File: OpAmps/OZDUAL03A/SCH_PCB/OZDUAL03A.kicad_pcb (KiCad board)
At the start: 2 copper layers, 40.4 x 40.4 mm, 53 parts, among them Con1 47u, Con2 47u, Con3 47u, Con4 47u, J1 JUMP2_2x1, J2 POWER, J3 OPAMPA, J4 OPAMPB, J5 SOT23-6, M1 HOLE, M2 HOLE, M3 HOLE, M4 HOLE, U1 OZ, U2 sot23-6

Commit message: Oprava, generování dat
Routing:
- net /VIN-: track 27.6 -> 30.9 mm
- net GNDA: track 198.2 -> 199.0 mm
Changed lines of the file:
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@@
-(kicad_pcb (version 4) (host pcbnew 4.0.5+dfsg1-4~bpo8+1)
+(kicad_pcb (version 20170123) (host pcbnew "(2017-02-05 revision 431abcf)-makepkg")
   (general
     (links 120)
     (no_connects 0)
-    (area 127.051999 76.251999 167.588001 116.788001)
+    (area 126.56552 69.817 180.212001 118.270714)
     (thickness 1.6)
     (drawings 48)
-    (tracks 401)
+    (tracks 412)
     (zones 0)
     (modules 53)
@@
   )
   (setup
-    (last_trace_width 0.254)
+    (last_trace_width 0.508)
     (user_trace_width 0.254)
     (user_trace_width 0.4572)
@@
     (visible_elements 7FFFFFFF)
     (pcbplotparams
-      (layerselection 0x011f0_80000001)
+      (layerselection 0x011f0_ffffffff)
       (usegerberextensions false)
       (excludeedgelayer true)
@@
       (hpglpenspeed 20)
       (hpglpendiameter 15)
-      (hpglpenoverlay 2)
       (psnegative false)
       (psa4output false)
@@
       (effects (font (size 1.5 1.5) (thickness 0.15)))
     )
-    (fp_text value POWER (at -3.556 0 360) (layer F.SilkS) hide
+    (fp_text value POWER (at -3.556 0) (layer F.SilkS) hide
       (effects (font (size 1.5 1.5) (thickness 0.15)))
     )
@@
     (tags "Diode SMA")
     (attr smd)
-    (fp_text reference Di1 (at -4.445 0 360) (layer F.SilkS)
+    (fp_text reference Di1 (at -4.445 0) (layer F.SilkS)
       (effects (font (size 1 1) (thickness 0.25)))
     )
@@
   (module Mlab_IO:SOT-23-6 (layer F.Cu)
     (at 147.193 105.664 270)
-    (fp_text reference U2 (at 1.99898 0 360) (layer F.SilkS) hide
+    (fp_text reference U2 (at 1.99898 0) (layer F.SilkS) hide
       (effects (font (size 0.762 0.762) (thickness 0.0762)))
     )
@@
   (segment (start 155.60802 83.947) (end 156.21 84.54898) (width 0.635) (layer F.Cu) (net 4))
   (segment (start 147.32 80.01) (end 147.32 82.55) (width 1.016) (layer F.Cu) (net 4))
+  (segment (start 163.83 91.44) (end 163.84 91.43) (width 0.508) (layer F.Cu) (net 5))
+  (segment (start 163.84 91.43) (end 165.19 91.43) (width 0.508) (layer F.Cu) (net 5))
+  (segment (start 165.19 91.43) (end 165.1635 91.4565) (width 0.508) (layer F.Cu) (net 5))
+  (segment (start 165.1635 91.4565) (end 165.1635 102.87) (width 0.508) (layer F.Cu) (net 5))
+  (segment (start 165.1635 102.87) (end 161.671 106.3625) (width 0.508) (layer F.Cu) (net 5))
+  (segment (start 161.671 106.3625) (end 158.75 106.3625) (width 0.508) (layer F.Cu) (net 5))
+  (segment (start 158.75 106.3625) (end 158.75 109.22) (width 0.508) (layer F.Cu) (net 5))
   (segment (start 143.51 102.1715) (end 143.256 102.1715) (width 0.508) (layer F.Cu) (net 5))
   (segment (start 143.256 102.1715) (end 142.24 103.1875) (width 0.508) (layer F.Cu) (net 5))
   (segment (start 142.24 103.1875) (end 142.24 105.3465) (width 0.508) (layer F.Cu) (net 5))
   (segment (start 142.24 105.3465) (end 140.97 106.6165) (width 0.508) (layer F.Cu) (net 5))
-  (segment (start 163.83 91.44) (end 165.1635 92.7735) (width 0.508) (layer F.Cu) (net 5))
-  (segment (start 161.671 106.3625) (end 158.75 106.3625) (width 0.508) (layer F.Cu) (net 5))
-  (segment (start 165.1635 102.87) (end 161.671 106.3625) (width 0.508) (layer F.Cu) (net 5))
-  (segment (start 165.1635 92.7735) (end 165.1635 102.87) (width 0.508) (layer F.Cu) (net 5))
   (segment (start 156.21 101.9175) (end 156.1465 101.9175) (width 0.508) (layer F.Cu) (net 5))
   (segment (start 156.1465 101.9175) (end 154.94 103.124) (width 0.508) (layer F.Cu) (net 5))
@@
   (via (at 154.94 89.916) (size 0.8) (drill 0.4) (layers F.Cu B.Cu) (net 5))
   (segment (start 154.94 89.916) (end 154.94 89.916) (width 0.635) (layer B.Cu) (net 5))
-  (segment (start 158.75 106.3625) (end 158.75 109.22) (width 0.508) (layer F.Cu) (net 5))
   (segment (start 158.75 109.22) (end 158.75 109.093) (width 0.45) (layer F.Cu) (net 5))
   (segment (start 157.48 110.49) (end 157.48 109.1565) (width 0.45) (layer F.Cu) (net 5))
@@
   (segment (start 142.24 80.01) (end 142.24 81.28) (width 1.016) (layer F.Cu) (net 5))
   (segment (start 142.24 81.28) (end 142.24 82.55) (width 1.016) (layer F.Cu) (net 5))
-  (segment (start 137.16 110.49) (end 137.16 109.4105) (width 0.508) (layer F.Cu) (net 6))
-  (segment (start 143.51 107.188) (end 143.51 106.3625) (width 0.508) (layer F.Cu) (net 6))
-  (segment (start 141.9225 108.7755) (end 143.51 107.188) (width 0.508) (layer F.Cu) (net 6))
-  (segment (start 137.795 108.7755) (end 141.9225 108.7755) (width 0.508) (layer F.Cu) (net 6))
-  (segment (start 137.16 109.4105) (end 137.795 108.7755) (width 0.508) (layer F.Cu) (net 6))
+  (segment (start 143.51 106.6165) (end 143.3195 106.6165) (width 0.508) (layer F.Cu) (net 6))
+  (segment (start 143.3195 106.6165) (end 141.316 108.62) (width 0.508) (layer F.Cu) (net 6))
+  (segment (start 141.316 108.62) (end 137.76 108.62) (width 0.508) (layer F.Cu) (net 6))
+  (segment (start 137.76 108.62) (end 137.16 109.22) (width 0.508) (layer F.Cu) (net 6))
+  (segment (start 137.16 109.22) (end 137.16 110.49) (width 0.508) (layer F.Cu) (net 6))
   (segment (start 148.336 94.615) (end 148.336 94.869) (width 0.635) (layer B.Cu) (net 6))
   (segment (start 137.16 109.22) (end 137.16 110.49) (width 0.635) (layer B.Cu) (net 6))
@@
   (segment (start 150.1775 87.58174) (end 149.87524 87.884) (width 0.635) (layer F.Cu) (net 6))
   (segment (start 150.1775 87.58174) (end 149.87524 87.884) (width 0.635) (layer F.Cu) (net 6))
+  (segment (start 144.14 83.91398) (end 143.85 83.91398) (width 0.635) (layer F.Cu) (net 7))
+  (segment (start 143.85 83.91398) (end 138.43 83.91398) (width 0.635) (layer F.Cu) (net 7))
+  (segment (start 144.78 82.7) (end 143.85 83.63) (width 0.508) (layer F.Cu) (net 7))
+  (segment (start 143.85 83.63) (end 143.85 83.91398) (width 0.508) (layer F.Cu) (net 7))
+  (segment (start 144.78 82.55) (end 144.78 82.7) (width 0.508) (layer F.Cu) (net 7))
+  (segment (start 144.55902 83.91398) (end 144.14 83.91398) (width 0.635) (layer F.Cu) (net 7))
+  (segment (start 144.78 83.15) (end 144.14 83.79) (width 0.508) (layer F.Cu) (net 7))
+  (segment (start 144.14 83.79) (end 144.14 83.91398) (width 0.508) (layer F.Cu) (net 7))
+  (segment (start 144.78 82.55) (end 144.78 83.15) (width 0.508) (layer F.Cu) (net 7))
   (segment (start 137.46 86.4) (end 136.12876 87.73124) (width 0.508) (layer F.Cu) (net 7))
   (segment (start 136.12876 87.73124) (end 136.12876 87.884) (width 0.4572) (layer F.Cu) (net 7))
@@
   (segment (start 144.78 83.439) (end 145.669 84.328) (width 1.016) (layer B.Cu) (net 7))
   (segment (start 144.78 82.55) (end 144.78 83.693) (width 0.635) (layer F.Cu) (net 7))
-  (segment (start 144.55902 83.91398) (end 138.43 83.91398) (width 0.635) (layer F.Cu) (net 7))
   (segment (start 138.43 83.91398) (end 138.43 84.59724) (width 0.635) (layer F.Cu) (net 7))
   (segment (start 149.86 80.01) (end 149.86 82.55) (width 1.016) (layer F.Cu) (net 7))
@@
   (segment (start 151.13 100.0125) (end 151.13 99.949) (width 0.635) (layer F.Cu) (net 14))
   (segment (start 161.29 99.06) (end 163.83 99.06) (width 1.016) (layer F.Cu) (net 14))
-  (segment (start 139.7 110.49) (end 139.7 109.855) (width 0.635) (layer B.Cu) (net 15))
-  (segment (start 139.7 109.855) (end 146.05 103.505) (width 0.635) (layer B.Cu) (net 15))
+  (segment (start 139.72 110.49) (end 146.05 104.16) (width 0.508) (layer B.Cu) (net 15))
+  (segment (start 146.05 104.16) (end 146.05 103.505) (width 0.508) (layer B.Cu) (net 15))
+  (segment (start 139.7 110.49) (end 139.72 110.49) (width 0.508) (layer B.Cu) (net 15))
   (via (at 146.05 103.505) (size 0.8) (drill 0.4) (layers F.Cu B.Cu) (net 15))
   (segment (start 146.05 104.5845) (end 146.05 104.267) (width 0.508) (layer F.Cu) (net 15) (status 10))

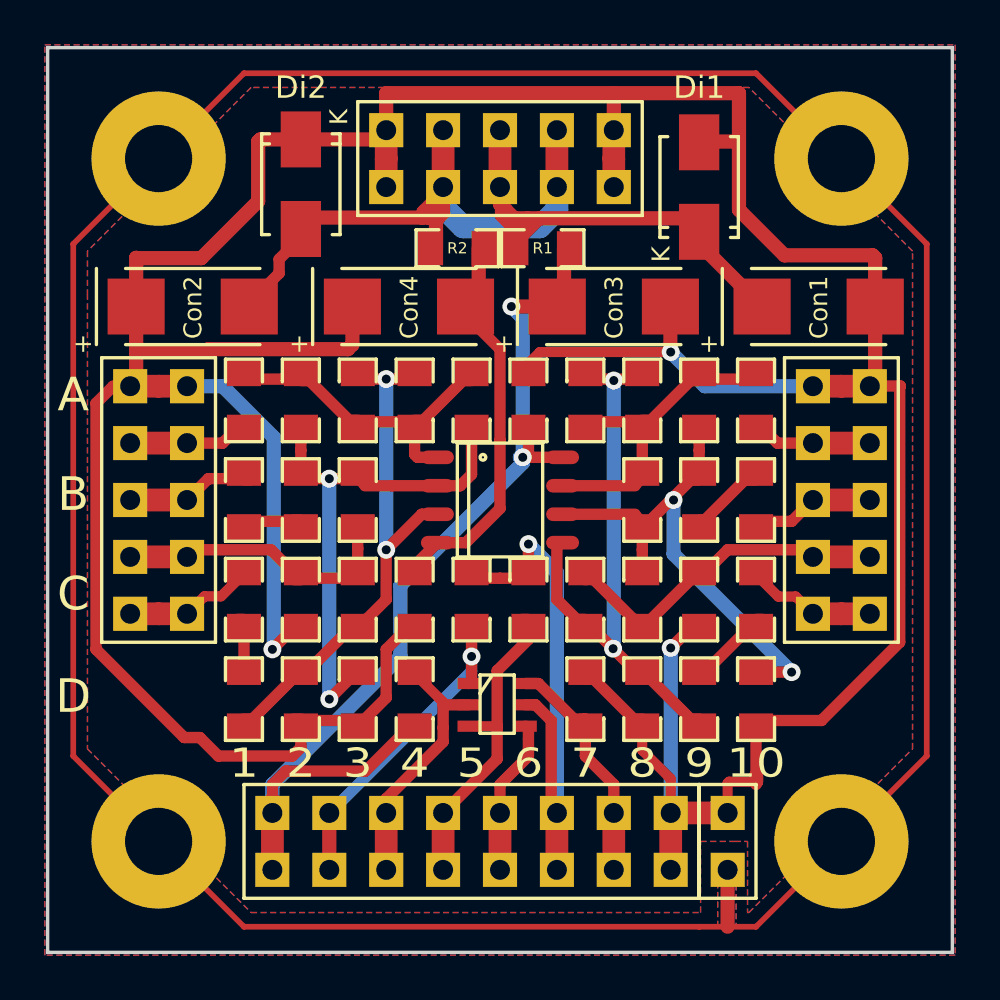
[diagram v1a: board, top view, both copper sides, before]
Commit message: OZDUAL03A module directory reverted to the condition before development of B  module revision.
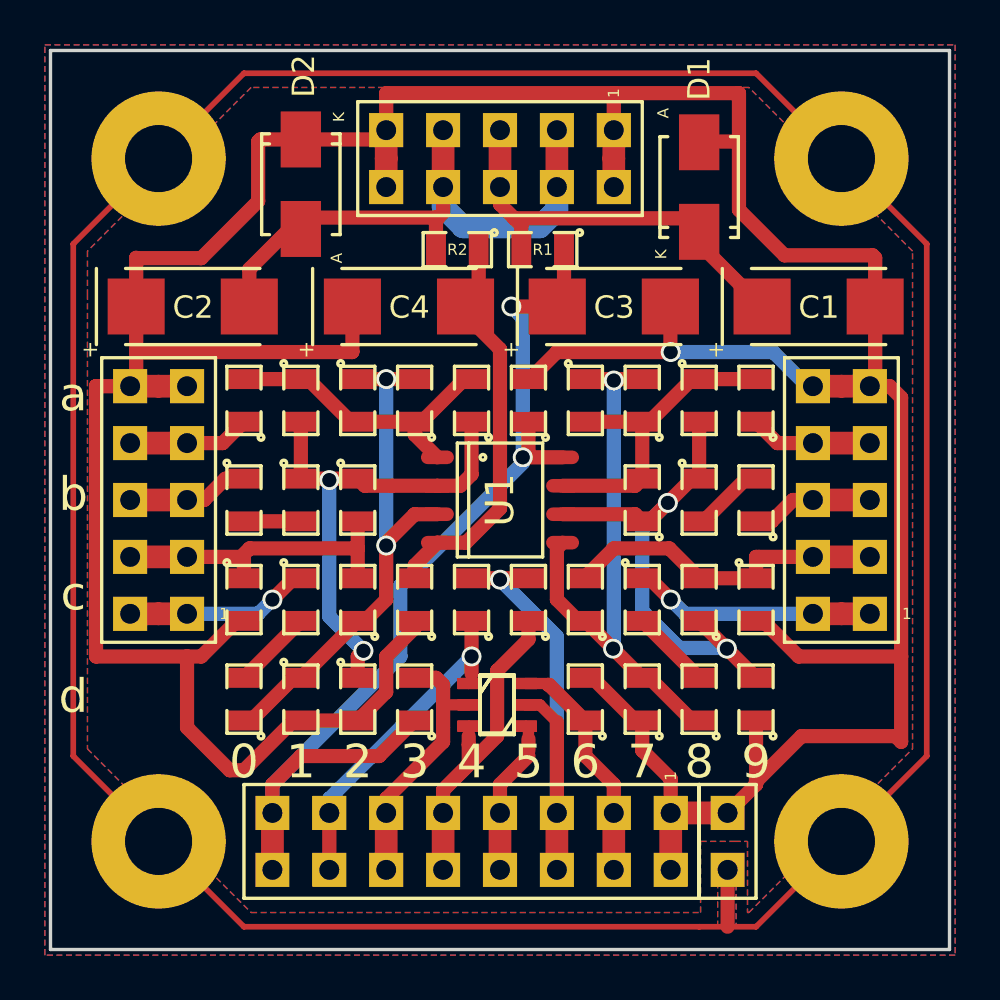
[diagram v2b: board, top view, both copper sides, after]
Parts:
- removed A1, A10, A3, A5, A7, B1, B10, B8, C10, C5, C6, C9: C, Mlab_R:SMD-0805-hand-soldering
- removed A2, A4, A8, A9, B2, B3, B9, C7, C8, D10, D3, D4, D7, D8, D9: R, Mlab_R:SMD-0805-hand-soldering
- removed A6: 100nF, Mlab_R:SMD-0805-hand-soldering
- removed the C1 at (135.9, 101.0)
- removed the C2 at (138.4, 101.0)
- removed the C3 at (141.0, 101.0)
- removed the C4 at (143.5, 101.0)
- removed the D1 at (135.9, 105.4)
- removed the D2 at (138.4, 105.4)
- added Q1: BC846, sot23-6:SOT-23-3, F.Cu at (147.2, 105.7)
- added U3: ANALOG SWITCH, Mlab_IO:SOT-23-6, F.Cu at (147.2, 105.7)
- added a0: C, Mlab_R:SMD-0805, F.Cu at (135.9, 92.1)
- added a1: R, Mlab_R:SMD-0805, F.Cu at (138.4, 92.1)
- added a2: C, Mlab_R:SMD-0805, F.Cu at (141.0, 92.1)
- added a3: R, Mlab_R:SMD-0805, F.Cu at (143.5, 92.1)
- added a4: C, Mlab_R:SMD-0805, F.Cu at (146.1, 92.1)
- added a5: 100nF, Mlab_R:SMD-0805, F.Cu at (148.6, 92.1)
- added a6: C, Mlab_R:SMD-0805, F.Cu at (151.1, 92.1)
- added a7: R, Mlab_R:SMD-0805, F.Cu at (153.7, 92.1)
- added a8: R, Mlab_R:SMD-0805, F.Cu at (156.2, 92.1)
- added a9: C, Mlab_R:SMD-0805, F.Cu at (158.8, 92.1)
- added b0: C, Mlab_R:SMD-0805, F.Cu at (135.9, 96.5)
- added b1: R, Mlab_R:SMD-0805, F.Cu at (138.4, 96.5)
- added b2: R, Mlab_R:SMD-0805, F.Cu at (141.0, 96.5)
- added b7: C, Mlab_R:SMD-0805, F.Cu at (153.7, 96.5)
- added b8: R, Mlab_R:SMD-0805, F.Cu at (156.2, 96.5)
- added b9: C, Mlab_R:SMD-0805, F.Cu at (158.8, 96.5)
- added c0: C, Mlab_R:SMD-0805, F.Cu at (135.9, 101.0)
- added c1: C, Mlab_R:SMD-0805, F.Cu at (138.4, 101.0)
- added c2: R, Mlab_R:SMD-0805, F.Cu at (141.0, 101.0)
- added c3: 100nF, Mlab_R:SMD-0805, F.Cu at (143.5, 101.0)
- added c4: C, Mlab_R:SMD-0805, F.Cu at (146.1, 101.0)
- added c5: C, Mlab_R:SMD-0805, F.Cu at (148.6, 101.0)
- added c6: R, Mlab_R:SMD-0805, F.Cu at (151.1, 101.0)
- added c7: C, Mlab_R:SMD-0805, F.Cu at (153.7, 101.0)
- added c8: R, Mlab_R:SMD-0805, F.Cu at (156.2, 101.0)
- added c9: C, Mlab_R:SMD-0805, F.Cu at (158.8, 101.0)
- added d0: R, Mlab_R:SMD-0805, F.Cu at (135.9, 105.4)
- added d1: R, Mlab_R:SMD-0805, F.Cu at (138.4, 105.4)
- added d2: R, Mlab_R:SMD-0805, F.Cu at (141.0, 105.4)
- added d3: R, Mlab_R:SMD-0805, F.Cu at (143.5, 105.4)
- added d6: R, Mlab_R:SMD-0805, F.Cu at (151.1, 105.4)
- added d7: R, Mlab_R:SMD-0805, F.Cu at (153.7, 105.4)
- added d8: R, Mlab_R:SMD-0805, F.Cu at (156.2, 105.4)
- added d9: R, Mlab_R:SMD-0805, F.Cu at (158.8, 105.4)
- R1, R2: footprint Mlab_R:SMD-0805-hand-soldering -> Mlab_R:SMD-0805
- U2: value sot23-6 -> MAX6066; footprint Mlab_IO:SOT-23-6 -> sot23-6:SOT-23-3
- moved R1 0.06 mm to (149.2, 85.3)
- moved R2 0.06 mm to (145.4, 85.3)
- renumbered Con1 to C1, Con2 to C2, Con3 to C3, Con4 to C4, Di1 to D1, Di2 to D2
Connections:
- U2 pad 2: /2 -> /3
- U2 pad 3: /3 -> /5
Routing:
- net GNDA: track 199.0 -> 188.6 mm, vias 3 -> 1
- net /VIN+: track 25.9 -> 18.7 mm
- net /INB+: track 5.74 -> 10.8 mm, vias 0 -> 1
- net Net-(C10-Pad2): track 3.91 -> 0.00 mm
- net Net-(c7-Pad2): track 0.00 -> 3.59 mm
- net Net-(c1-Pad2): track 0.00 -> 3.59 mm
- net /VIN-: track 30.9 -> 27.5 mm
- net Net-(b8-Pad2): track 0.00 -> 3.33 mm
- net Net-(B10-Pad2): track 3.33 -> 0.00 mm
- net Net-(b0-Pad2): track 0.00 -> 2.86 mm
- net Net-(B1-Pad2): track 2.86 -> 0.00 mm
- net Net-(C1-Pad2): track 2.86 -> 0.00 mm
- net /INA+: track 5.74 -> 8.28 mm, vias 0 -> 1
- net /5: track 24.8 -> 22.4 mm
- net Net-(U1-Pad2): track 24.9 -> 22.6 mm
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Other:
- board size 40.4 x 40.4 mm -> 40.1 x 40.1 mm
- net class Default: clearance 0.15 -> 0.2
- rule trace_clearance: 0.15 -> 0.2
- rule via_min_size: 0.4 -> 0.7
- board text added: "0"
- board text added: "a"
- board text added: "b"
- board text added: "c"
- board text added: "d"
- board text removed: "10"
- board text removed: "A"
- board text removed: "B"
- board text removed: "C"
- board text removed: "D"

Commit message: uprava potisku
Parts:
- removed Q1: BC846, sot23-6:SOT-23-3
- removed U3: ANALOG SWITCH, Mlab_IO:SOT-23-6
- removed c4, c5: C, Mlab_R:SMD-0805
- removed d3, d6: R, Mlab_R:SMD-0805
- added C5: C, Mlab_R:SMD-0805, F.Cu at (146.1, 101.0)
- added C6: C, Mlab_R:SMD-0805, F.Cu at (148.6, 101.0)
- added D4: R, Mlab_R:SMD-0805, F.Cu at (143.5, 105.4)
- added D7: R, Mlab_R:SMD-0805, F.Cu at (151.1, 105.4)
- U2: value MAX6066 -> sot23-6; footprint sot23-6:SOT-23-3 -> Mlab_IO:SOT-23-6
- renumbered a0 to A1, a9 to A10, a1 to A2, a2 to A3, a3 to A4, a4 to A5, a5 to A6, a6 to A7, a7 to A8, a8 to A9, b0 to B1, b9 to B10, b1 to B2, b2 to B3, b7 to B8, b8 to B9, c0 to C1, c9 to C10, c1 to C2, c2 to C3, c3 to C4, c6 to C7, c7 to C8, c8 to C9, C1 to Con1, C2 to Con2, C3 to Con3, C4 to Con4, d0 to D1, d9 to D10, d2 to D3, d7 to D8, d8 to D9, D1 to Di1, D2 to Di2
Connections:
- U2 pad 2: /3 -> /2
- U2 pad 3: /5 -> /3
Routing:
- net /3: track 16.7 -> 14.7 mm
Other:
- board size 40.1 x 40.1 mm -> 40.4 x 40.4 mm
- rule via_min_size: 0.7 -> 0.4
- board text added: "10"
- board text added: "A"
- board text added: "B"
- board text added: "C"
- board text added: "D"
- board text removed: "0"
- board text removed: "a"
- board text removed: "b"
- board text removed: "c"
- board text removed: "d"

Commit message: zvetseni plosek
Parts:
- removed d1: R, Mlab_R:SMD-0805
- added D2: R, Mlab_R:SMD-0805-hand-soldering, F.Cu at (138.4, 105.4)
- A1, A10, A2, A3, A4, A5, A6, A7, A8, A9, B1, B10, B2, B3, B8, B9, C1, C10, C2, C3, C4, C5, C6, C7, D1, D10, D3, D4, D7, D8, D9, R1, R2: footprint Mlab_R:SMD-0805 -> Mlab_R:SMD-0805-hand-soldering
- C8: value C -> R; footprint Mlab_R:SMD-0805 -> Mlab_R:SMD-0805-hand-soldering
- C9: value R -> C; footprint Mlab_R:SMD-0805 -> Mlab_R:SMD-0805-hand-soldering
- moved R1 0.06 mm to (149.2, 85.3)
- moved R2 0.06 mm to (145.4, 85.3)
- turned C9 to 270 degrees
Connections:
- C1 pad 1: /VREFA -> /INA+
- C1 pad 2: GNDA -> Net-(C1-Pad2)
- C10 pad 1: /VREFB -> /INB+
- C10 pad 2: GNDA -> Net-(C10-Pad2)
- C2 pad 1: /INA+ -> /VREFA
- C2 pad 2: Net-(C2-Pad2) -> GNDA
- C8 pad 1: /INB+ -> Net-(A9-Pad2)
- C8 pad 2: Net-(C8-Pad2) -> /VREFB
- C9 pad 1: Net-(A9-Pad2) -> /VREFB
- C9 pad 2: /VREFB -> GNDA
- D1 pad 2: Net-(C2-Pad2) -> Net-(C1-Pad2)
- D9 pad 2: Net-(C8-Pad2) -> Net-(C10-Pad2)
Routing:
- net GNDA: track 188.6 -> 198.5 mm, vias 1 -> 3
- net /INB+: track 10.8 -> 5.74 mm, vias 1 -> 0
- net Net-(C10-Pad2): track 0.00 -> 3.91 mm
- net Net-(C8-Pad2): track 3.59 -> 0.00 mm
- net Net-(C2-Pad2): track 3.59 -> 0.00 mm
- net Net-(C1-Pad2): track 0.00 -> 2.86 mm
- net Net-(A2-Pad2): track 22.6 -> 25.3 mm
- net /INA+: track 8.28 -> 5.74 mm, vias 1 -> 0
- net Net-(A3-Pad1): track 24.4 -> 26.9 mm
- net /5: track 22.4 -> 24.8 mm
- net Net-(A1-Pad2): track 13.7 -> 14.3 mm
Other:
- net class Default: clearance 0.2 -> 0.15
- rule trace_clearance: 0.2 -> 0.15

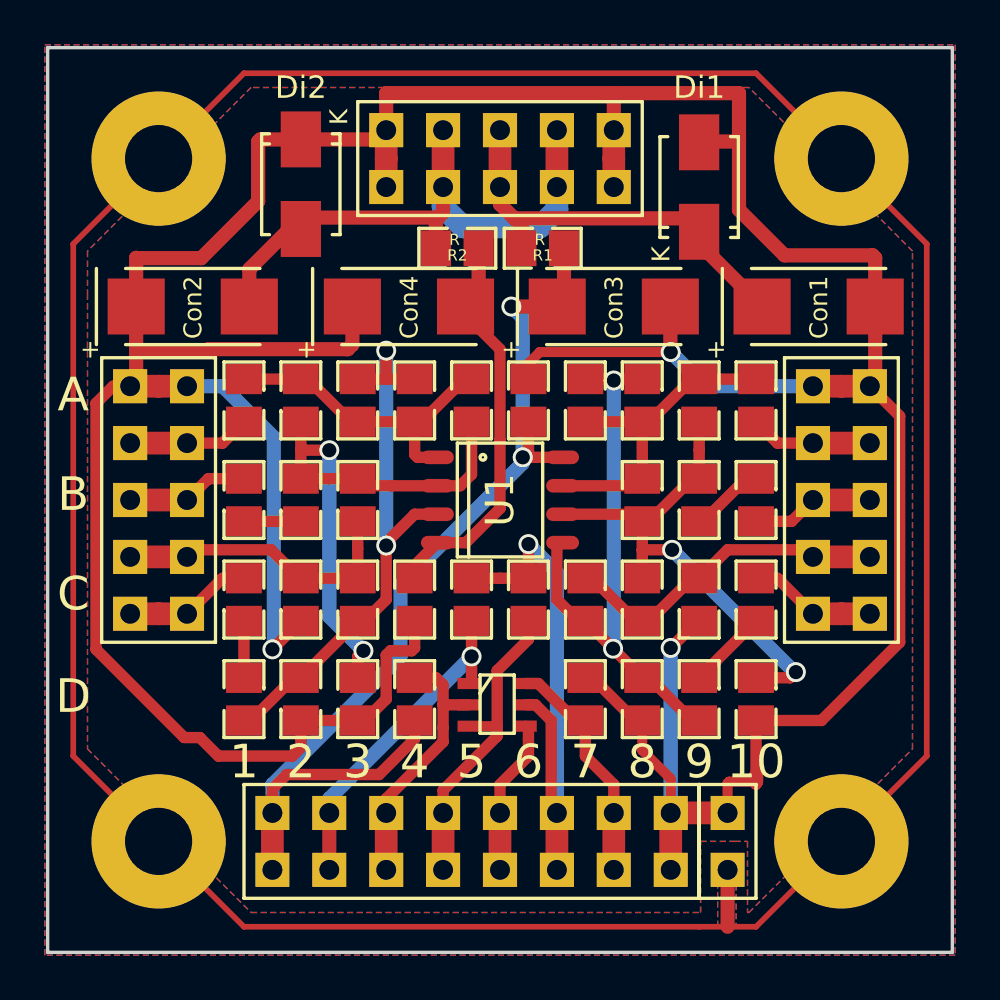
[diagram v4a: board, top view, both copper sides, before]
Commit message: uprava cest
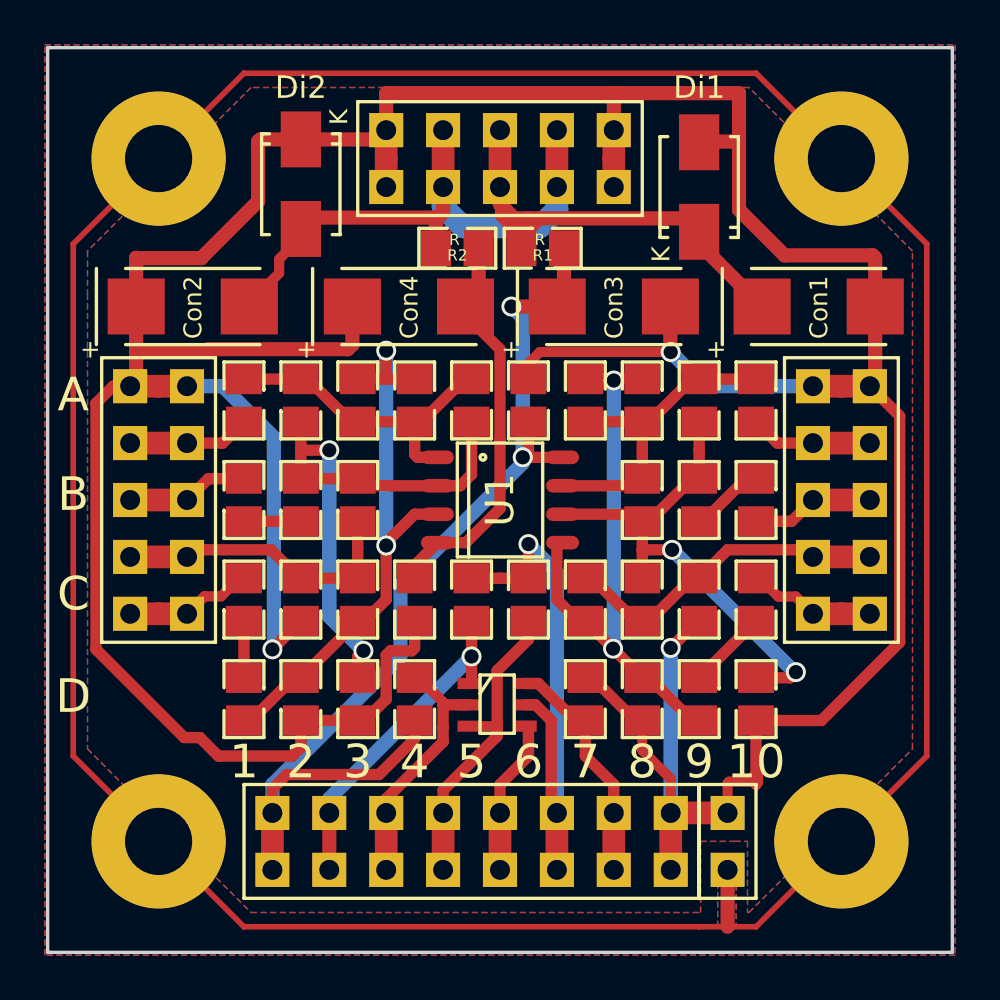
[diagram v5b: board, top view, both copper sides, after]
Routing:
- net /VIN+: track 18.7 -> 25.9 mm
